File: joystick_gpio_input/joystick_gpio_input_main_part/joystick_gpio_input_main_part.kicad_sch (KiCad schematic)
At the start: 22 parts, among them J1 Conn_01x06, J12 Conn_01x15, J2 Conn_01x04, J3 Conn_01x15, J4 Conn_01x15, J5 Conn_01x14

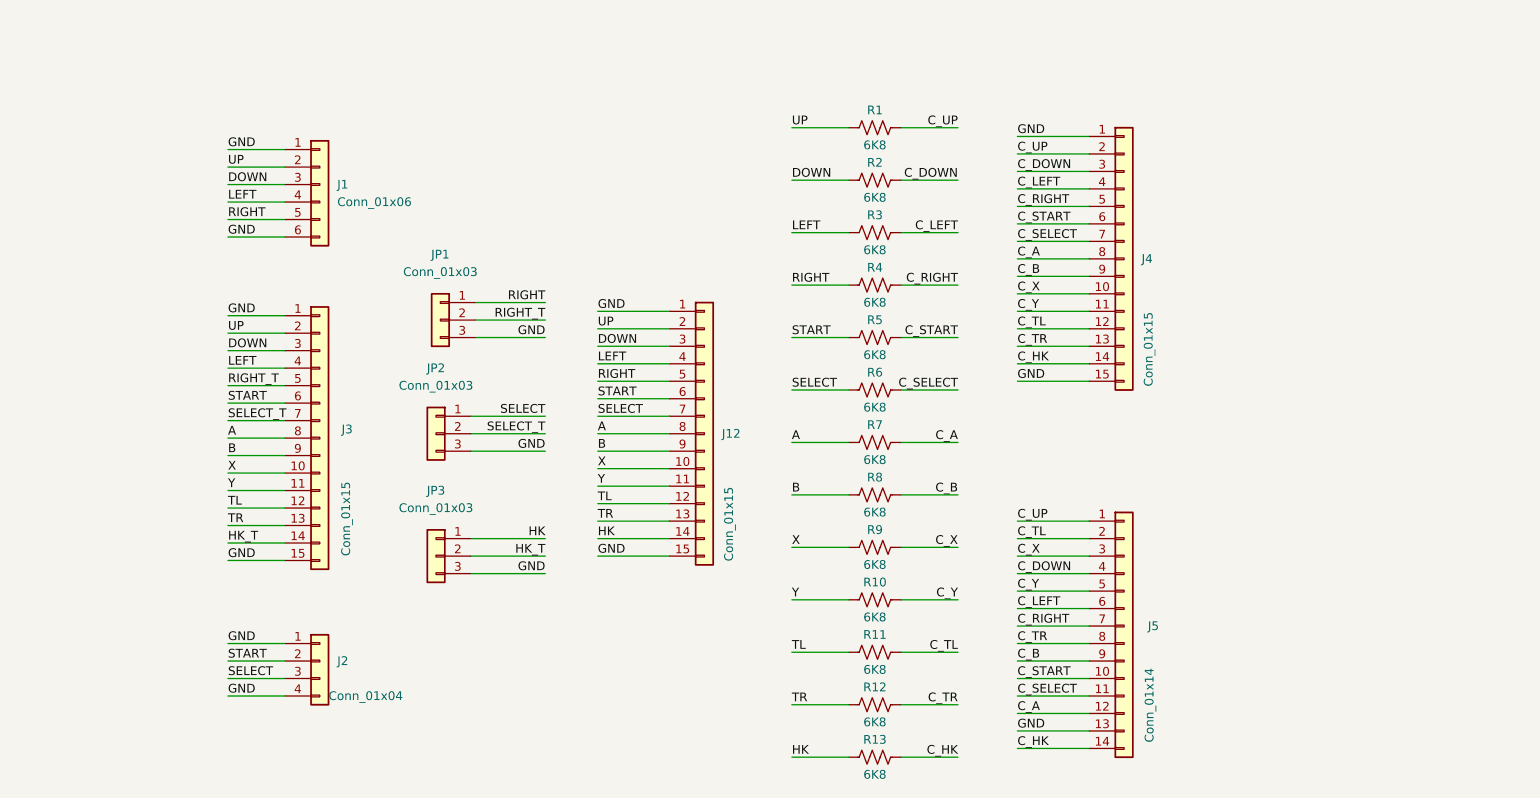
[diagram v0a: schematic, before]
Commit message: joystick gpio 스크린샷 추가
Signed-off-by: Ju, Gyeong-min <jcmh74@gmail.com>
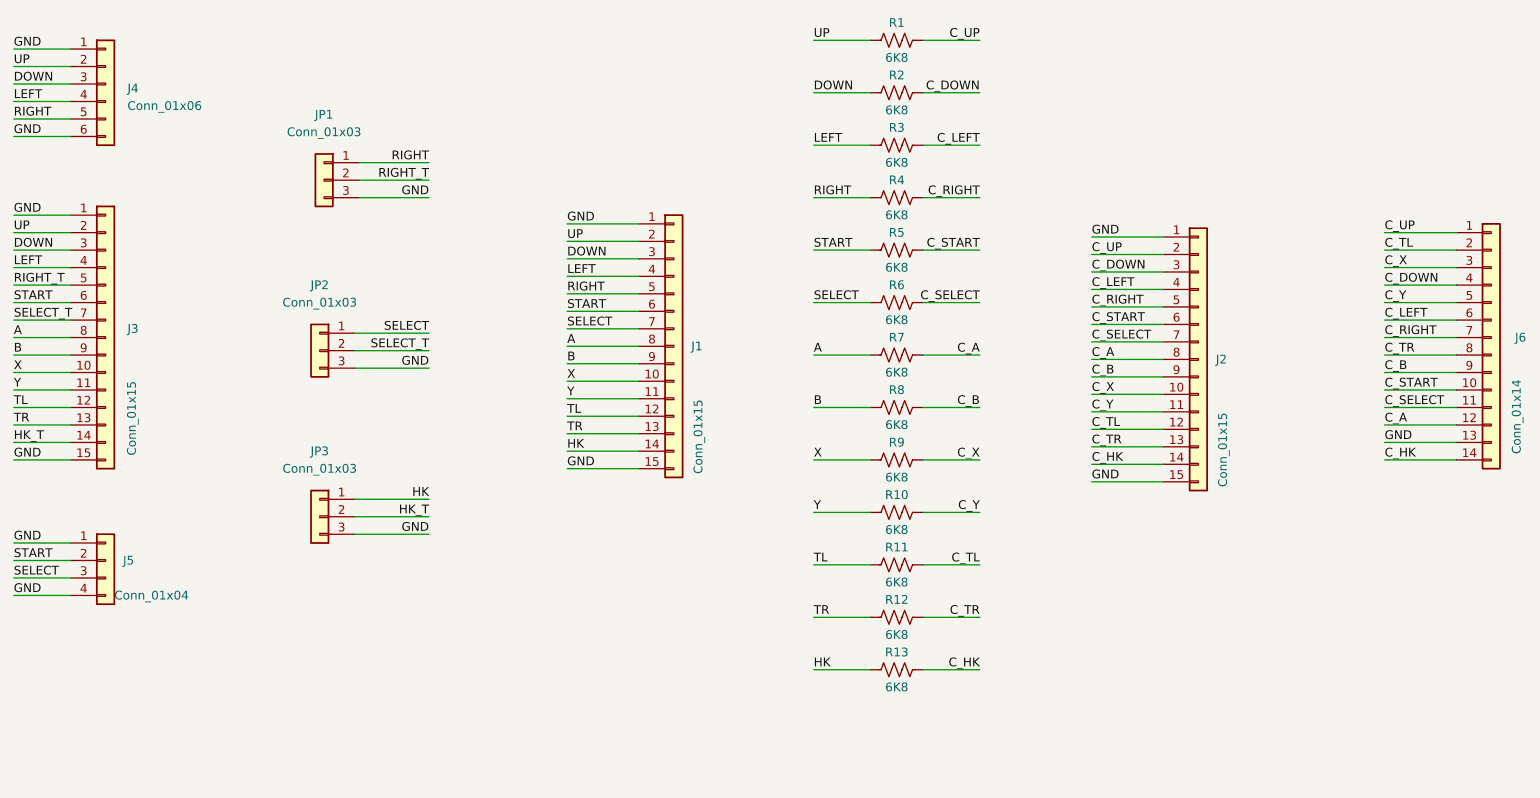
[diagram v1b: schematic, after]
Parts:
- renumbered J12 to J1, J4 to J2, J1 to J4, J2 to J5, J5 to J6
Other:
- title: Raspberry Pie GPIO Input Module -> Raspberry Pie GPIO Input Module (Main Part)
- moved on the sheet: J1, J2, J3, J4, J5, J6, JP1, JP2, JP3, R1, R10, R11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
